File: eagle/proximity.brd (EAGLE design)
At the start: 72.4 x 66 mm, 13 parts

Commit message: added PCB file
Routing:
- net PR3_ECHO: track 25.6 -> 13.1 mm
- net DISPL_DB4: track 53.8 -> 61.8 mm, vias 1 -> 0
- net DISPL_DB7: track 68.2 -> 61.6 mm
- net DISPL_DB6: track 71.0 -> 73.1 mm
- net DISPL_E: track 52.6 -> 54.3 mm
- net N$3: track 23.3 -> 21.7 mm
- net DISPL_DB5: track 66.0 -> 67.2 mm
- net +5V: track 119.8 -> 121.0 mm
- net DISPL_RS: track 45.6 -> 44.7 mm

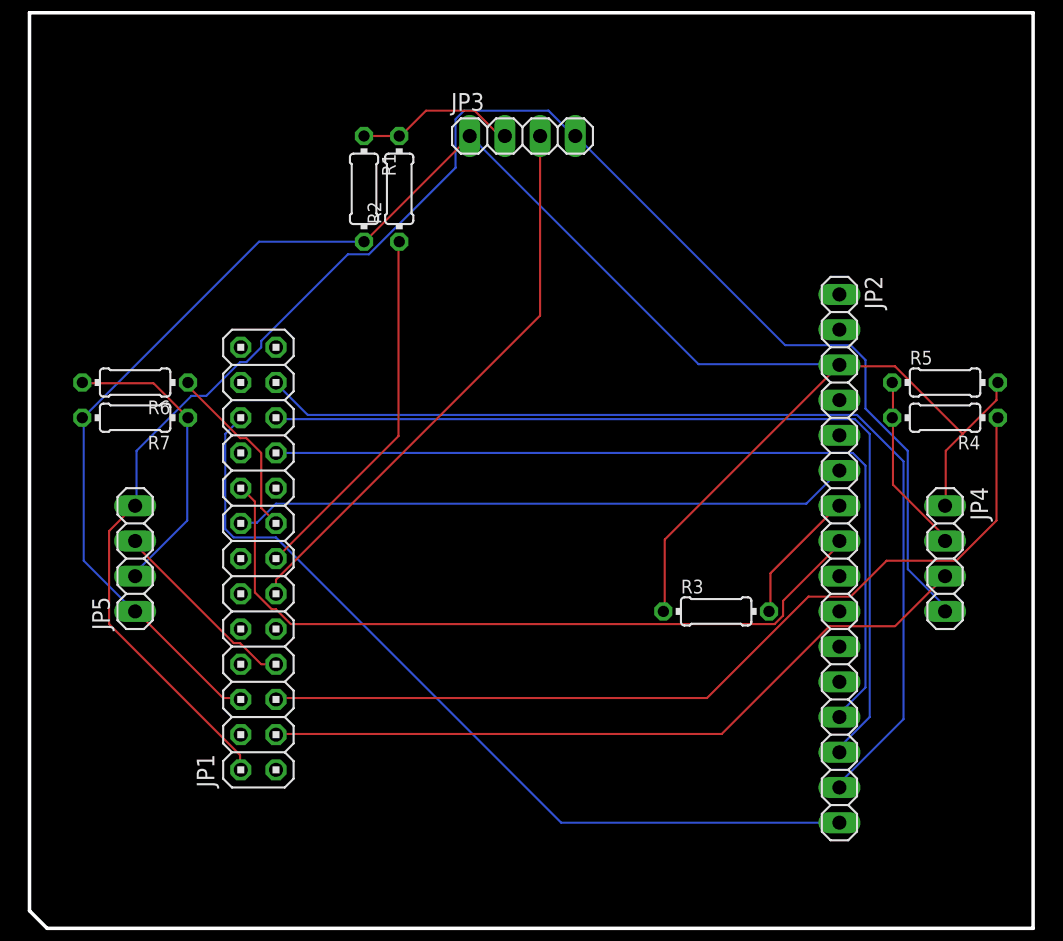
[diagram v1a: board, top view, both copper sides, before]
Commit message: added GND and +5V planes
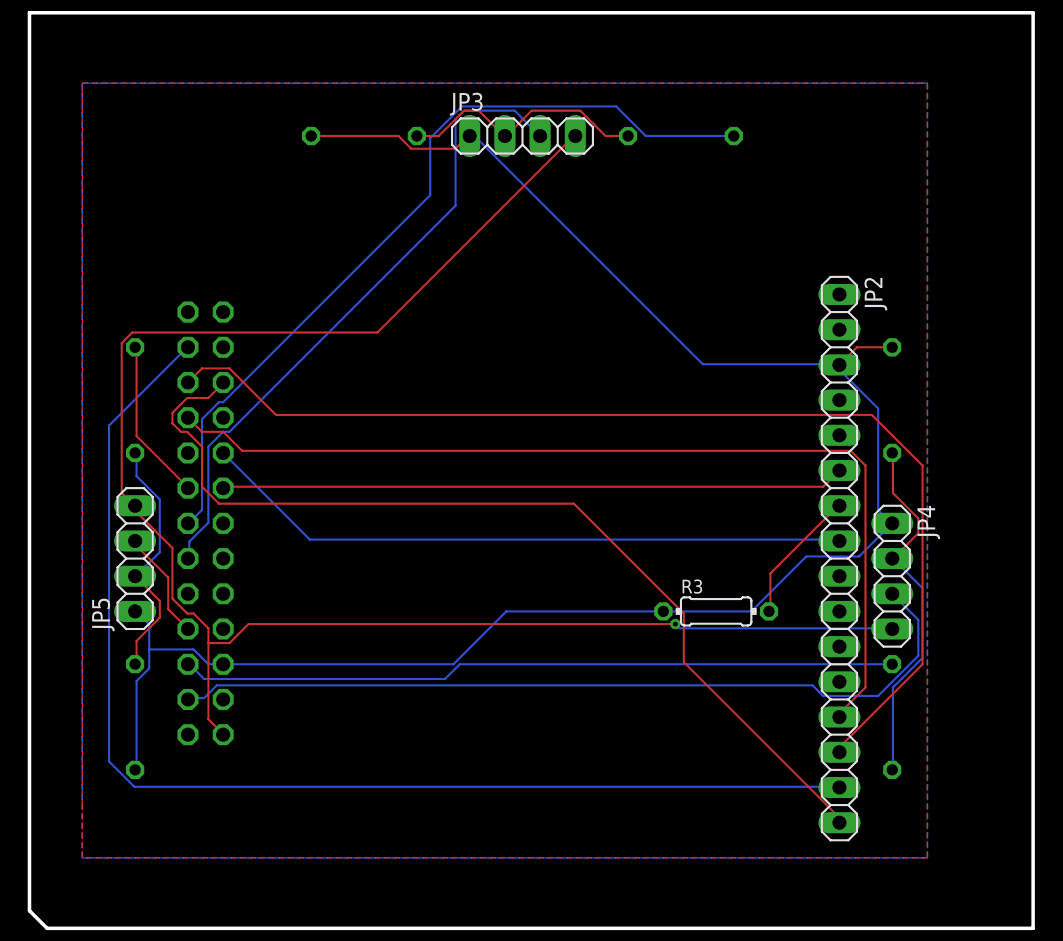
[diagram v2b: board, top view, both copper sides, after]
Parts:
- moved R4 21.9 mm to (63.5, 26.7), flipped to the bottom, turned to 270 degrees
- moved R7 21.6 mm to (8.89, 26.7), flipped to the bottom, turned to 270 degrees
- moved R2 20.7 mm to (48.3, 68.6), flipped to the bottom, turned to 0 degrees
- moved JP1 4.58 mm to (14.0, 40.6), flipped to the bottom
- moved JP4 4.02 mm to (63.5, 36.8)
- moved R5 4.02 mm to (63.5, 49.5), flipped to the bottom, turned to 90 degrees
- moved R1 3.81 mm to (25.4, 68.6), flipped to the bottom, turned to 0 degrees
- moved R6 1.27 mm to (8.89, 49.5), flipped to the bottom, turned to 270 degrees
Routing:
- net PR1_ECHO: track 26.6 -> 59.0 mm
- net N$2: track 13.0 -> 26.3 mm
- net PR2_ECHO: track 64.8 -> 51.7 mm
- net DISPL_DB6: track 73.1 -> 85.7 mm
- net DISPL_DB5: track 67.2 -> 79.5 mm
- net DISPL_DB7: track 61.6 -> 69.4 mm
- net DISPL_DB4: track 61.8 -> 69.2 mm
- net DISPL_E: track 54.3 -> 47.1 mm
- net PR2_TRIGGER: track 53.0 -> 59.9 mm
- net GND: track 140.4 -> 133.7 mm
- net N$1: track 11.7 -> 18.3 mm
- net PR1_TRIGGER: track 40.9 -> 47.1 mm
- net PR3_TRIGGER: track 14.0 -> 7.95 mm
- net N$3: track 21.7 -> 18.3 mm
- net PR3_ECHO: track 13.1 -> 11.8 mm
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- added copper zone on layer 1, net GND
- added copper zone on layer 16, net N$4
- added copper zone on layer 16, net N$5

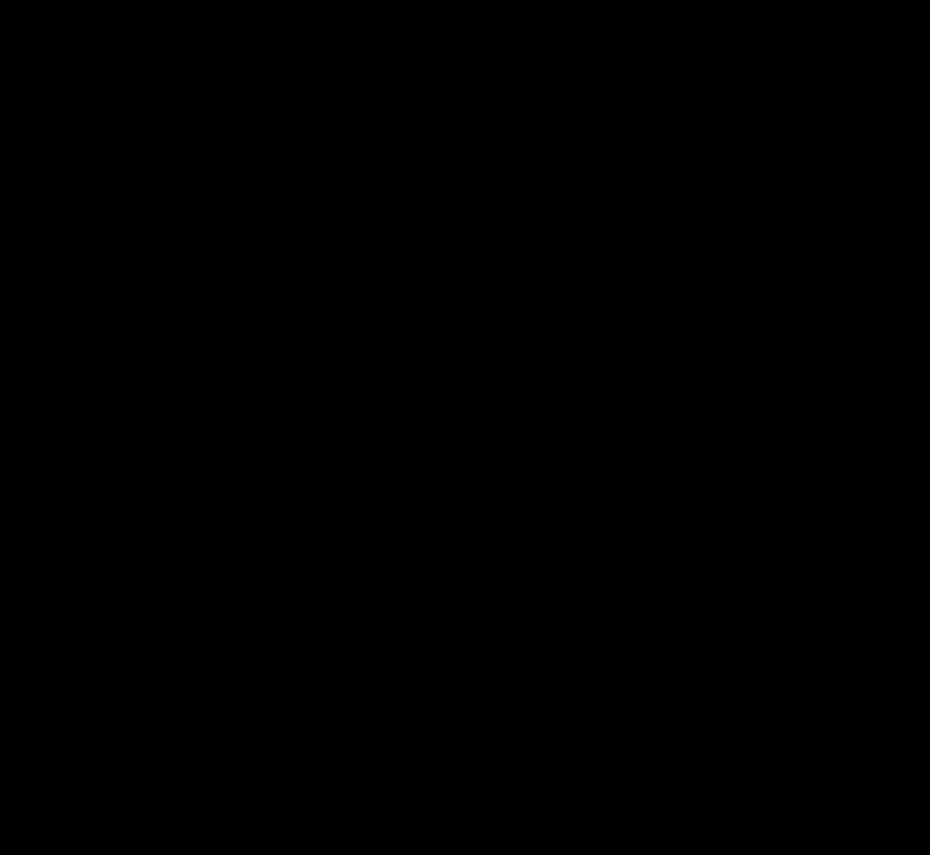
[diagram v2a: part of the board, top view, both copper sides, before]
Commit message: added USB to serial to schematic
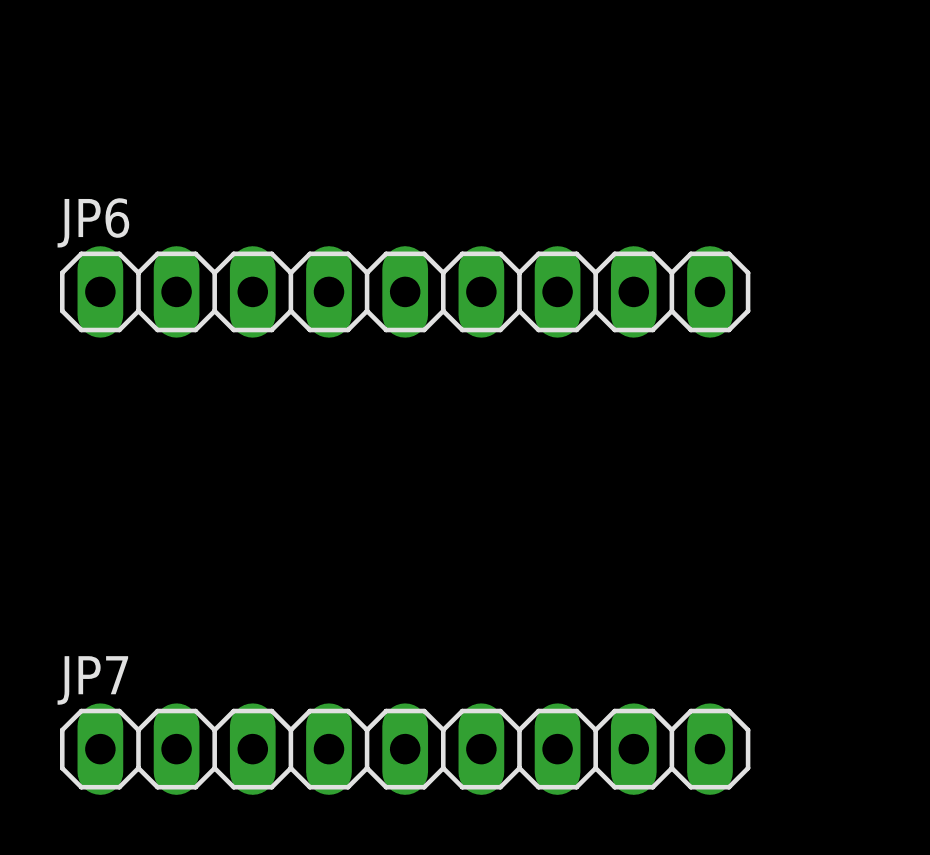
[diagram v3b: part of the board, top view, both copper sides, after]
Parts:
- added JP6, JP7: (no value), pinhead:1X09
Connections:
- new net DBG_RX: JP1.10, JP6.2
- new net DBG_TX: JP1.8, JP6.3
- new net N$10: JP6.8, JP6.9
- net +5V: now also JP6.7
- net GND: now also JP6.1
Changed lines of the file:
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@@
 <?xml version="1.0" encoding="utf-8"?>
 <!DOCTYPE eagle SYSTEM "eagle.dtd">
-<eagle version="8.4.0">
+<eagle version="8.4.1">
 <drawing>
 <settings>
@@
 <param name="dpMaxLengthDifference" value="10mm"/>
 <param name="dpGapFactor" value="2.5"/>
+<param name="checkAngle" value="0"/>
 <param name="checkFont" value="1"/>
 <param name="checkRestrict" value="1"/>
@@
 <element name="R7" library="resistor" library_urn="urn:adsk.eagle:library:348" package="0204/7" package3d_urn="urn:adsk.eagle:package:25945/1" value="2k" x="8.89" y="26.67" rot="MR270"/>
 <element name="JP5" library="pinhead" library_urn="urn:adsk.eagle:library:325" package="1X04" package3d_urn="urn:adsk.eagle:package:22407/2" value="" x="8.89" y="38.1" rot="R90"/>
+<element name="JP6" library="pinhead" library_urn="urn:adsk.eagle:library:325" package="1X09" package3d_urn="urn:adsk.eagle:package:22483/1" value="" x="-82.55" y="2.54"/>
+<element name="JP7" library="pinhead" library_urn="urn:adsk.eagle:library:325" package="1X09" package3d_urn="urn:adsk.eagle:package:22483/1" value="" x="-82.55" y="-12.7"/>
 </elements>
 <signals>
@@
 <vertex x="5.08" y="16.51"/>
 </polygon>
+<contactref element="JP6" pad="1"/>
+<wire x1="8.89" y1="22.86" x2="-92.71" y2="2.54" width="0" layer="19" extent="1-1"/>
 </signal>
 <signal name="+5V">
@@
 <wire x1="8.8392" y1="41.91" x2="8.89" y2="41.91" width="0.1524" layer="1"/>
 <via x="47.8536" y="33.3756" extent="1-16" drill="0.35"/>
+<contactref element="JP6" pad="7"/>
+<wire x1="7.9248" y1="42.8244" x2="-77.47" y2="2.54" width="0" layer="19" extent="1-1"/>
 </signal>
 <signal name="N$2">
@@
 </polygon>
 </signal>
+<signal name="N$10">
+<contactref element="JP6" pad="8"/>
+<contactref element="JP6" pad="9"/>
+<wire x1="-72.39" y1="2.54" x2="-74.93" y2="2.54" width="0" layer="19" extent="1-1"/>
+</signal>
+<signal name="DBG_TX">
+<contactref element="JP1" pad="8"/>
+<contactref element="JP6" pad="3"/>
+<wire x1="15.24" y1="33.02" x2="-87.63" y2="2.54" width="0" layer="19" extent="1-1"/>
+</signal>
+<signal name="DBG_RX">
+<contactref element="JP1" pad="10"/>
+<contactref element="JP6" pad="2"/>
+<wire x1="15.24" y1="35.56" x2="-90.17" y2="2.54" width="0" layer="19" extent="1-1"/>
+</signal>
 </signals>

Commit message: echo IRQ is shared because it is used by different gpio pins
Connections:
- net GND: now also JP2.5
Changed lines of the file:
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@@
 </polygon>
 <contactref element="JP6" pad="1"/>
-<wire x1="8.89" y1="22.86" x2="-92.71" y2="2.54" width="0" layer="19" extent="1-1"/>
+<contactref element="JP2" pad="5"/>
+<wire x1="62.484" y1="48.9204" x2="59.69" y2="46.99" width="0" layer="19" extent="16-16"/>
+<wire x1="-92.71" y1="2.54" x2="8.89" y2="22.86" width="0" layer="19" extent="1-1"/>
 </signal>
 <signal name="+5V">
